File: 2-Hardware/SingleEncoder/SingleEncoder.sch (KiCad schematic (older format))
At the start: 26 parts, among them J1 PMOD_SINGLE, P1 CONN_01X06, Q1 MMBT2222, Q2 MMBT2222, U1 TPS60131, U2 MCP6L02, U3 ILD213T

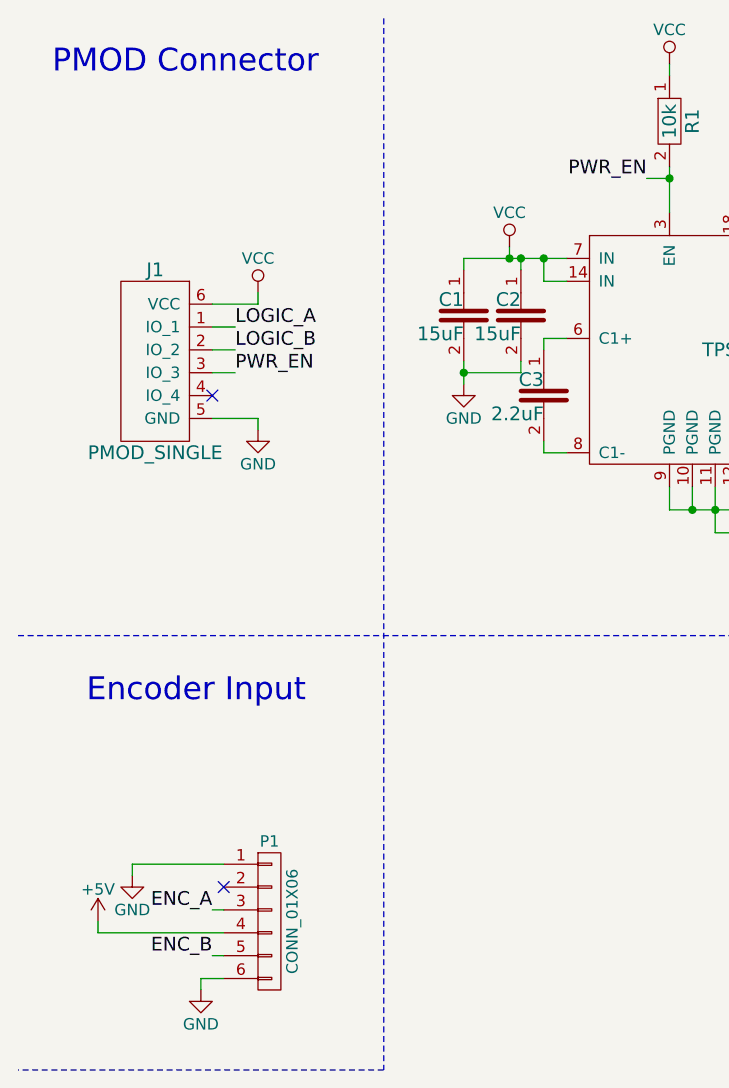
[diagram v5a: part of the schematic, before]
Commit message: Added 4-pin connector behind the DIN connector
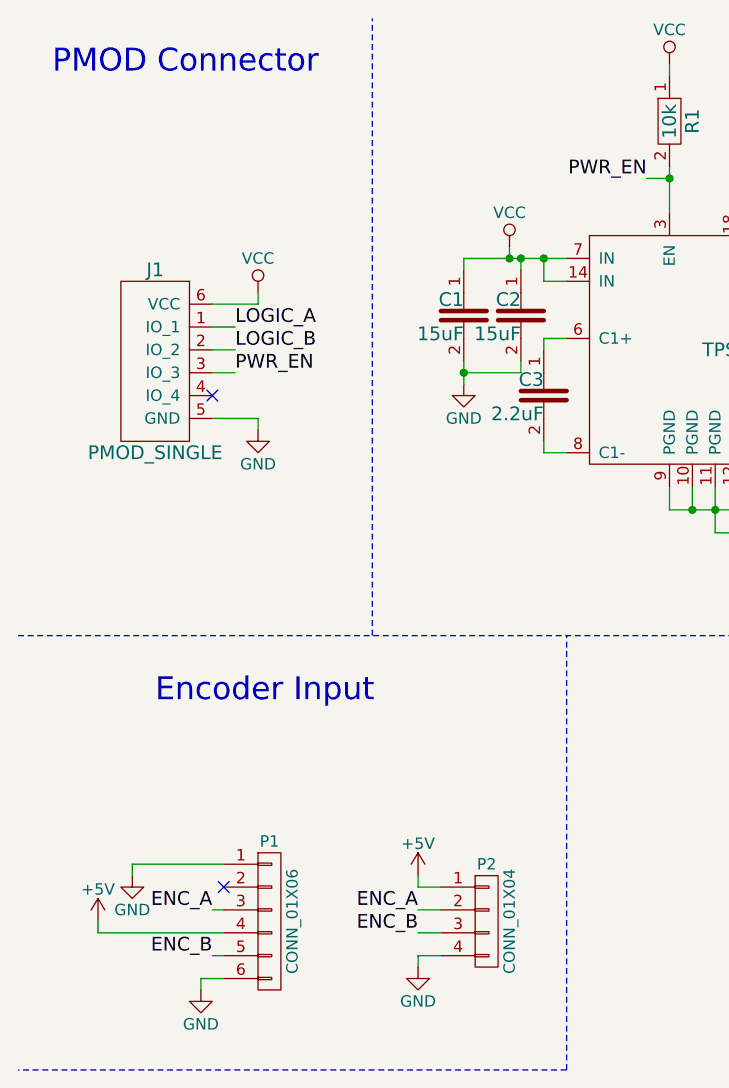
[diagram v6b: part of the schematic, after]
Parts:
- added P2: CONN_01X04, Connectors:CONN_2.54mm_1x4, symbol CONN_01X04
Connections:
- net +5V: now also P2.1 (P1)
- net ENC_A: now also P2.2 (P2)
- net ENC_B: now also P2.3 (P3)
- net GND: now also P2.4 (P4)
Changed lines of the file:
@@
 Wire Wire Line
 	1400 4600 1350 4600
-Text Notes 800  3500 0    100  ~ 0
+Text Notes 1100 3500 0    100  ~ 0
 Encoder Input
 $Comp
@@
 Wire Notes Line
 	6100 4400 11200 4400
-Wire Notes Line
-	2100 500  2100 5100
-Wire Notes Line
-	2100 5100 500  5100
 $Comp
 L RES R2
@@
 Wire Wire Line
 	3550 2750 3850 2750
+$Comp
+L CONN_01X04 P2
+U 1 1 55BC4992
+P 2550 4450
+F 0 "P2" H 2550 4700 50  0000 C CNN
+F 1 "CONN_01X04" V 2650 4450 50  0000 C CNN
+F 2 "Connectors:CONN_2.54mm_1x4" H 2550 4450 60  0001 C CNN
+F 3 "" H 2550 4450 60  0000 C CNN
+	1    2550 4450
+	1    0    0    -1
+$EndComp
+$Comp
+L GND #PWR027
+U 1 1 55BC4AA2
+P 2250 4650
+F 0 "#PWR027" H 2250 4400 50  0001 C CNN
+F 1 "GND" H 2250 4500 50  0000 C CNN
+F 2 "" H 2250 4650 60  0000 C CNN
+F 3 "" H 2250 4650 60  0000 C CNN
+	1    2250 4650
+	1    0    0    -1
+$EndComp
+$Comp
+L +5V #PWR028
+U 1 1 55BC4AF0
+P 2250 4250
+F 0 "#PWR028" H 2250 4100 50  0001 C CNN
+F 1 "+5V" H 2250 4390 50  0000 C CNN
+F 2 "" H 2250 4250 60  0000 C CNN
+F 3 "" H 2250 4250 60  0000 C CNN
+	1    2250 4250
+	1    0    0    -1
+$EndComp
+Text Label 2250 4400 2    60   ~ 0
+ENC_A
+Text Label 2250 4500 2    60   ~ 0
+ENC_B
+Wire Wire Line
+	2350 4600 2250 4600
+Wire Wire Line
+	2250 4600 2250 4650
+Wire Wire Line
+	2250 4500 2350 4500
+Wire Wire Line
+	2350 4400 2250 4400
+Wire Wire Line
+	2250 4250 2250 4300
+Wire Wire Line
+	2250 4300 2350 4300
+Wire Notes Line
+	2050 3200 2050 500
+Wire Notes Line
+	2900 5100 2900 3200
+Wire Notes Line
+	2900 5100 500  5100
 $EndSCHEMATC

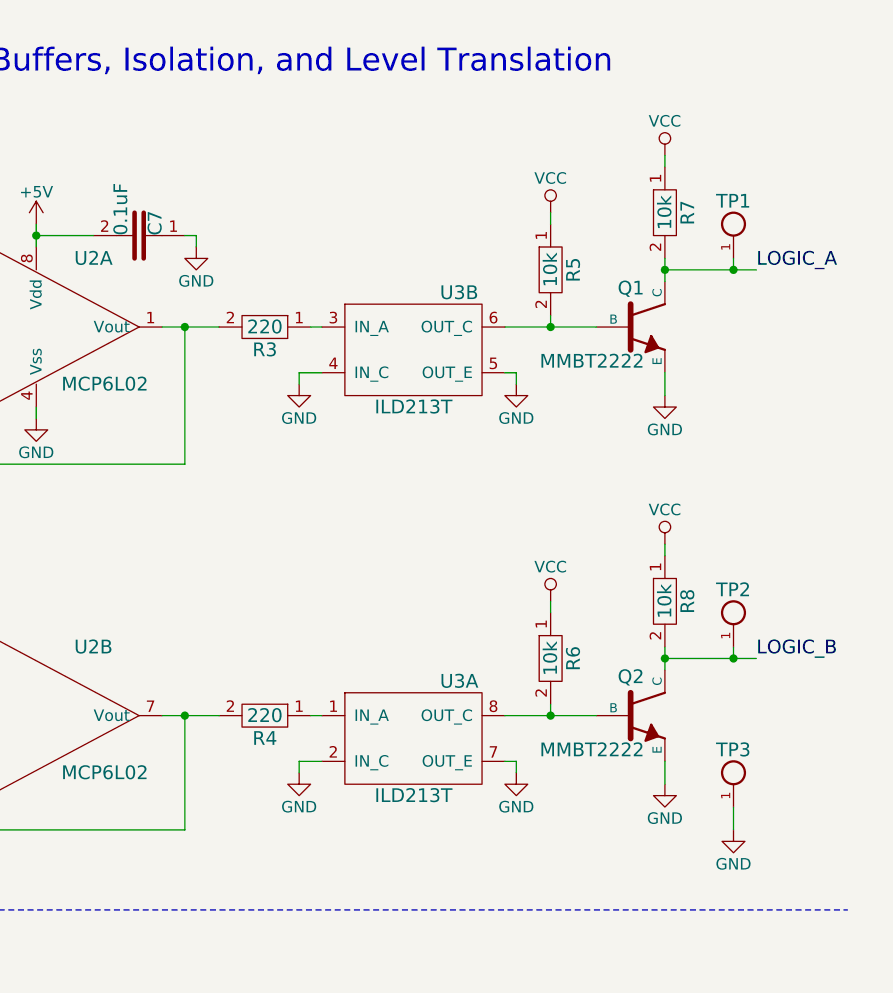
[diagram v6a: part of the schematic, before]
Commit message: Replaced Opto-isolator with I2C level shifter
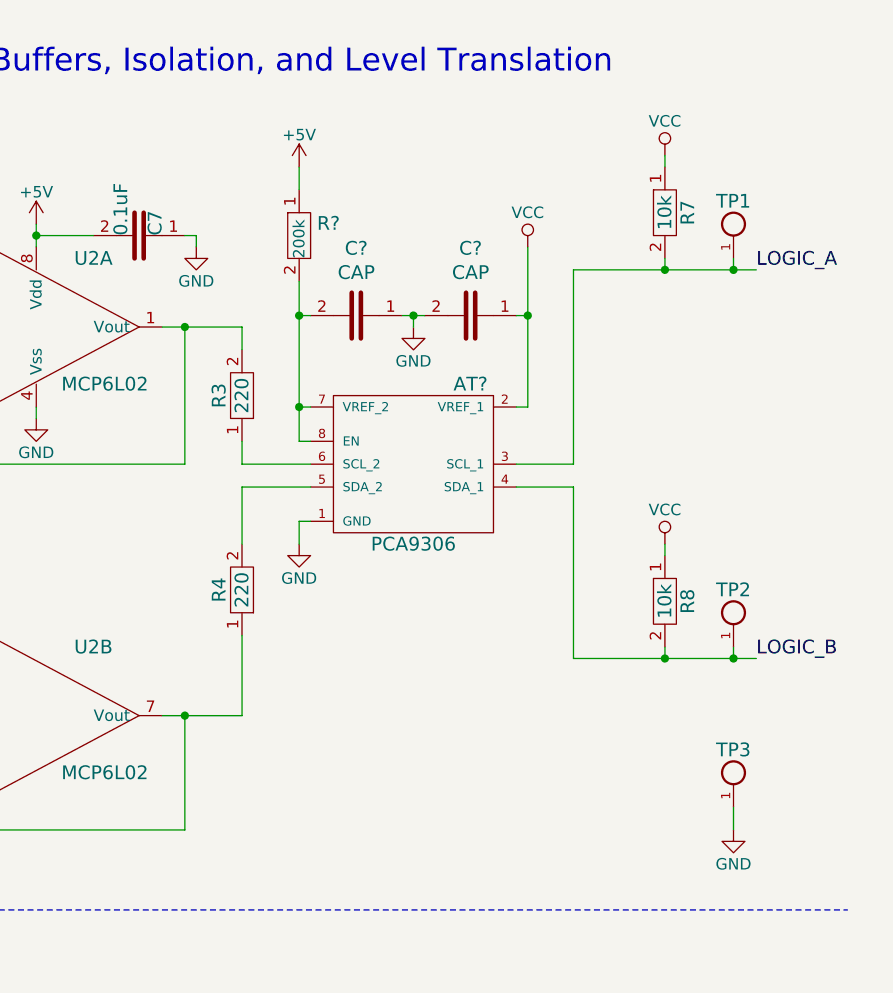
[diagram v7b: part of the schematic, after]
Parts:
- removed Q1, Q2: MMBT2222, Transistors:TRANS_SOT-23-3_BEC, symbol NPN_3-Term
- removed R5, R6: 10k, SMD:SMD_0805, symbol RES
- removed U3: ILD213T, SMD:SOIC_08_4.0mm_5.8mm_1.27mm, symbol ILD213T
- added AT?: PCA9306, symbol PCA9306
- added C? (x2): CAP, symbol CAP
- added R?: 200k, symbol RES
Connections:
- net +5V: now also R?.1
- net GND: now also AT?.1 (GND), C?.1, C?.2
- net LOGIC_A: now also AT?.3 (SCL_1)
- net LOGIC_B: now also AT?.4 (SDA_1)
- net VCC: now also AT?.2 (VREF_1), C?.1
- net at U2.6 (-), U2.7 (Vout): now also R4.1; no longer R4.2
- net at R3.1: now also AT?.6 (SCL_2)
- new net: AT?.5 (SDA_2), R4.2
- new net: AT?.7 (VREF_2), AT?.8 (EN), C?.2, R?.2
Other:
- moved on the sheet: R3, R4

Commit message: Changed level translator
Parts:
- removed AT?: PCA9306, symbol PCA9306
- removed C? (x2): CAP, symbol CAP
- removed R7, R8: 10k, SMD:SMD_0805, symbol RES
- removed R?: 200k, symbol RES
- removed U2: MCP6L02, SMD:SSOP_08_3.0mm_3.0mm_0.65mm, symbol MCP6L02
- added AT1: TXB0102, symbol TXB0102
- added C8: CAP, SMD:SMD_0805, symbol CAP
- added D2, D3: PLVA653A, Diodes:DIODE_SOT-23-3, symbol D_ZENER
- C7: value 0.1uF -> CAP; DigikeyNumber 311-1141-1-ND -> (none); Manufacturer Yageo -> (none); ManufacturerNumber CC0805KRX7R8BB104 -> (none)
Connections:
- net labels added: EN
- net labels removed: PWR_EN
- wire segments 115 -> 93
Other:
- moved on the sheet: R3, R4, TP1, TP2, TP3
